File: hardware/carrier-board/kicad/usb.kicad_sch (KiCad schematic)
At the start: 5 parts, among them J11 backpack uplink, J40 RP2350 audio, J41 knob/LoRa, J42 VITURE/cam, U7 USB2514B

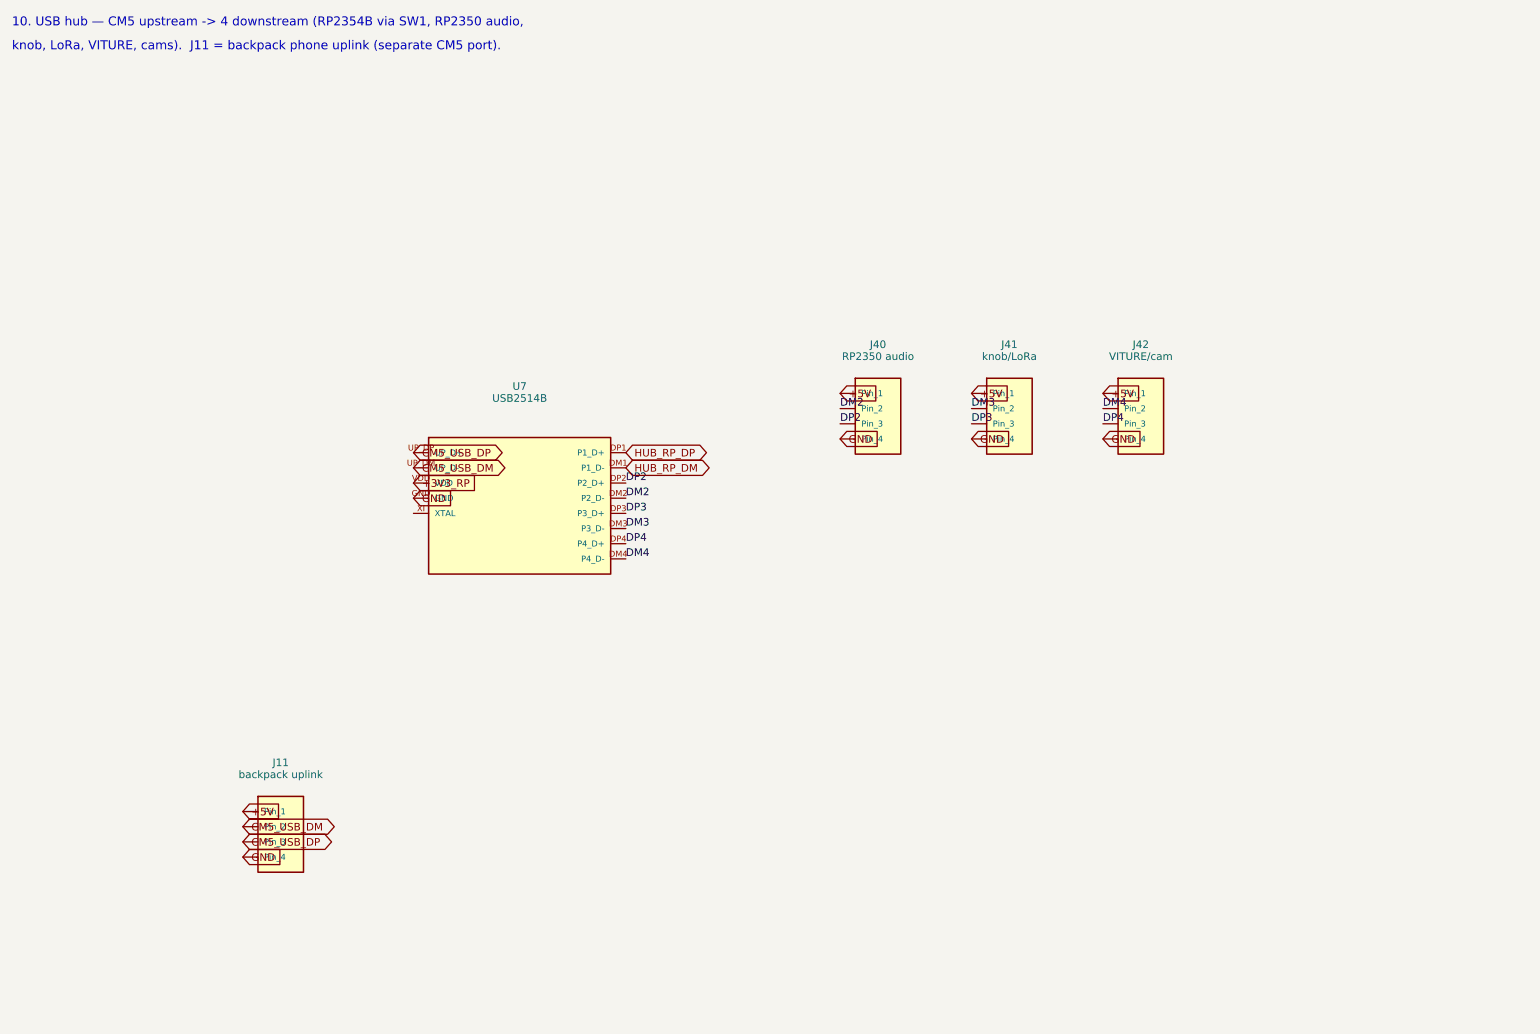
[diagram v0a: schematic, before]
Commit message: hardware(carrier): replace USB 2.0 hub with VL817 USB 3.1 4-port hub
Swap the on-board USB2514B (USB 2.0) for a VIA VL817 4-port USB 3.1 Gen1
(5 Gbps) hub with four USB-C downstream receptacles (J40-J43), upstream on
a CM5 USB 3.0 port. The CM5 exposes 2x USB 3.0 + 1x USB 2.0, so:

  - USB3 #0 -> VL817 upstream (SuperSpeed + USB 2.0)
  - USB3 #1 -> RP2354B CDC (now OFF-hub, via SW1) -> frees all 4 hub ports
  - USB2    -> backpack phone uplink (J11)

Generator (populate_sheets.py):
  - new VL817 condensed symbol (USB2 + SS per port, xtal, reset, straps)
  - new USB-C 3.1 receptacle symbol (VBUS/GND/CC/D+-/one SS lane)
  - CM5 symbol gains USB3 SuperSpeed pins + 2nd/3rd USB ports
  - rewrite sh_usb(): per-port CC Rp pull-ups (56k, host/DFP), VBUS PTC off
    +5V, USBLC6 ESD, SS AC-coupling caps at each TX, 25 MHz hub clock
  - SW1 'A' side rerouted from hub to the dedicated CM5 USB port

Docs: CONNECTORS, POWER, BOM, REQUIREMENTS, BLOCK-DIAGRAM, READMEs updated
for the USB 3.1 hub, USB-C downstream ports, and off-hub RP2354B link.

All 11 sheets regenerated; S-expressions balanced and cross-sheet global
nets verified consistent.

Co-Authored-By: Claude Opus 4.8 <noreply@anthropic.com>
Claude-Session: https://claude.ai/code/session_01DgiE5SHRCeyk1gvfvshMGa
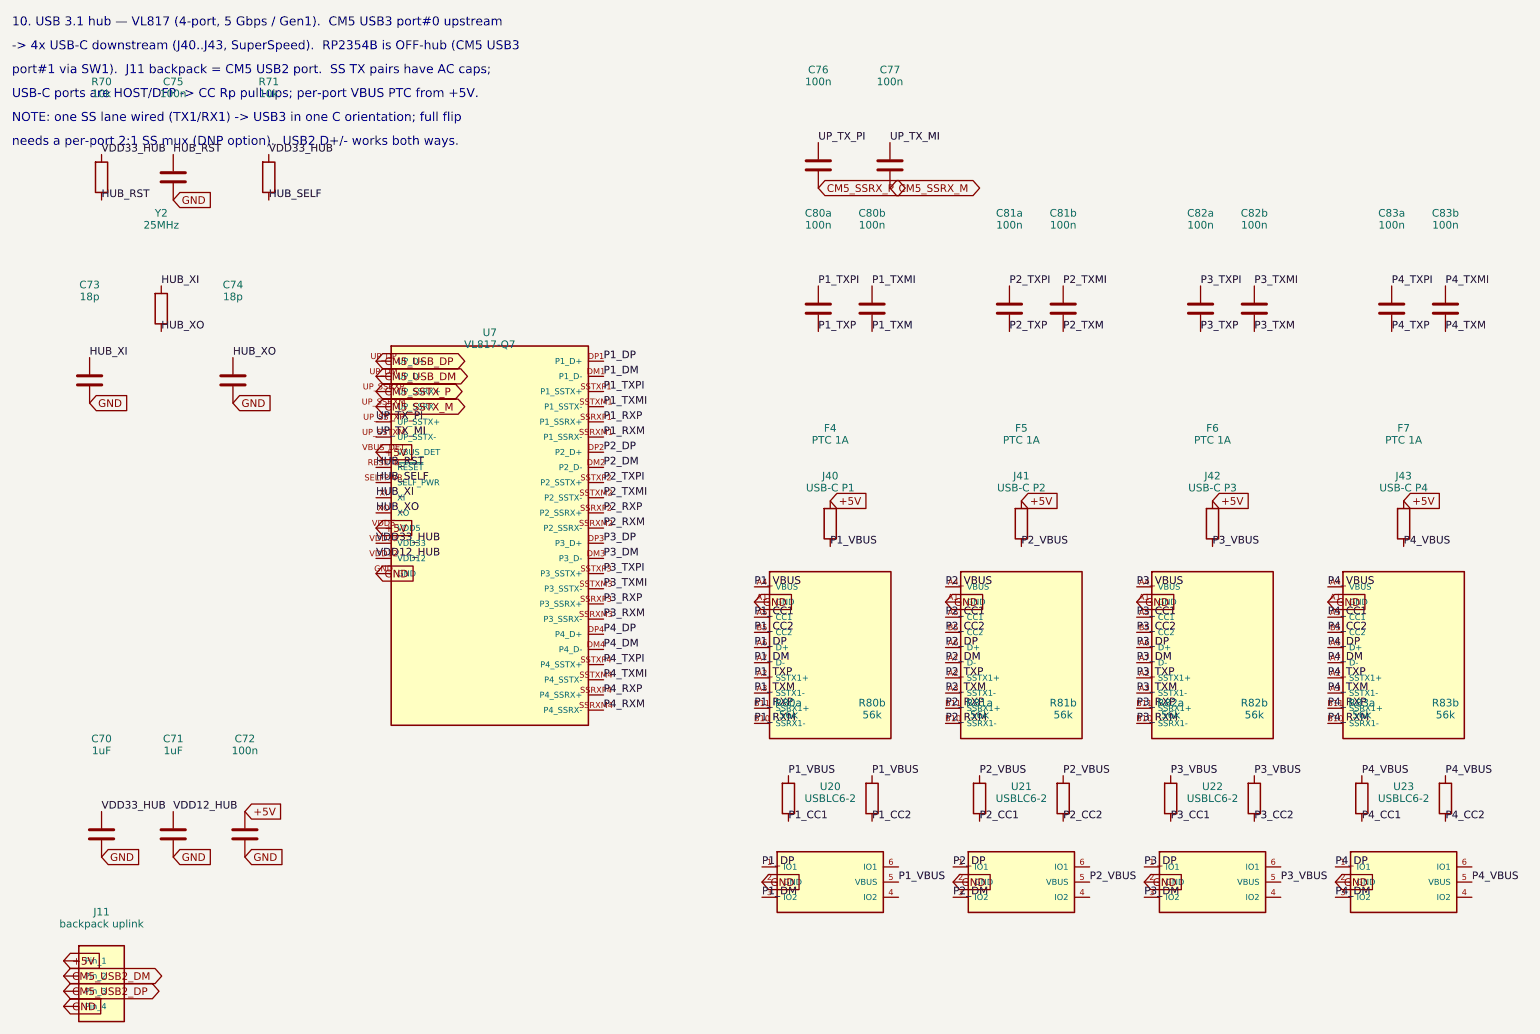
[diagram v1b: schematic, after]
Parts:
- removed J40: RP2350 audio, symbol Connector_Generic:Conn_01x04
- removed J41: knob/LoRa, symbol Connector_Generic:Conn_01x04
- removed J42: VITURE/cam, symbol Connector_Generic:Conn_01x04
- removed U7: USB2514B, symbol Interface_USB:USB2514B
- added C70, C71: 1uF, symbol Device:C
- added C72, C75, C76, C77, C80a, C80b, C81a, C81b, C82a, C82b, C83a, C83b: 100n, symbol Device:C
- added C73, C74: 18p, symbol Device:C
- added F4, F5, F6, F7: PTC 1A, symbol Device:Fuse
- added J40: USB-C P1, symbol Connector:USB_C_Receptacle_USB3.1
- added J41: USB-C P2, symbol Connector:USB_C_Receptacle_USB3.1
- added J42: USB-C P3, symbol Connector:USB_C_Receptacle_USB3.1
- added J43: USB-C P4, symbol Connector:USB_C_Receptacle_USB3.1
- added R70, R71: 10k, symbol Device:R
- added R80a, R80b, R81a, R81b, R82a, R82b, R83a, R83b: 56k, symbol Device:R
- added U20, U21, U22, U23: USBLC6-2, symbol Interface_USB:USBLC6-2SC6
- added U7: VL817-Q7, symbol Interface_USB:VL817
- added Y2: 25MHz, symbol Device:Crystal
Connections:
- net +5V: now also C72.1, F4.1, F5.1, F6.1, F7.1, U7.VBUS_DET, U7.VDD5
- net CM5_USB_DM: now also U7.UP_DM (UP_D-); no longer J11.2 (Pin_2)
- net CM5_USB_DP: now also U7.UP_DP (UP_D+); no longer J11.3 (Pin_3)
- net GND: now also C70.2, C71.2, C72.2, C73.2, C74.2, C75.2, J40.A1 (GND), J41.A1 (GND), J42.A1 (GND), J43.A1 (GND), U20.2 (GND), U21.2 (GND), U22.2 (GND), U23.2 (GND), U7.GND
- new net CM5_SSRX_M: C77.2
- new net CM5_SSRX_P: C76.2
- new net CM5_SSTX_M: U7.UP_SSRXM (UP_SSRX-)
- new net CM5_SSTX_P: U7.UP_SSRXP (UP_SSRX+)
- new net CM5_USB2_DM: J11.2 (Pin_2)
- new net CM5_USB2_DP: J11.3 (Pin_3)
- new net HUB_RST: C75.1, R70.2, U7.RESETB (~{RESET})
- new net HUB_SELF: R71.2, U7.SELFPWR (SELF_PWR)
- new net HUB_XI: C73.1, U7.XI, Y2.1
- new net HUB_XO: C74.1, U7.XO, Y2.2
- new net P1_CC1: J40.A5 (CC1), R80a.2
- new net P1_CC2: J40.B5 (CC2), R80b.2
- new net P1_DM: J40.A7 (D-), U20.3 (IO2), U7.DM1 (P1_D-)
- new net P1_DP: J40.A6 (D+), U20.1 (IO1), U7.DP1 (P1_D+)
- new net P1_RXM: J40.B10 (SSRX1-), U7.SSRXM1 (P1_SSRX-)
- new net P1_RXP: J40.B11 (SSRX1+), U7.SSRXP1 (P1_SSRX+)
- new net P1_TXM: C80b.2, J40.A3 (SSTX1-)
- new net P1_TXMI: C80b.1, U7.SSTXM1 (P1_SSTX-)
- new net P1_TXP: C80a.2, J40.A2 (SSTX1+)
- new net P1_TXPI: C80a.1, U7.SSTXP1 (P1_SSTX+)
- new net P1_VBUS: F4.2, J40.A4 (VBUS), R80a.1, R80b.1, U20.5 (VBUS)
- new net P2_CC1: J41.A5 (CC1), R81a.2
- new net P2_CC2: J41.B5 (CC2), R81b.2
- new net P2_DM: J41.A7 (D-), U21.3 (IO2), U7.DM2 (P2_D-)
- new net P2_DP: J41.A6 (D+), U21.1 (IO1), U7.DP2 (P2_D+)
- new net P2_RXM: J41.B10 (SSRX1-), U7.SSRXM2 (P2_SSRX-)
- new net P2_RXP: J41.B11 (SSRX1+), U7.SSRXP2 (P2_SSRX+)
- new net P2_TXM: C81b.2, J41.A3 (SSTX1-)
- new net P2_TXMI: C81b.1, U7.SSTXM2 (P2_SSTX-)
- new net P2_TXP: C81a.2, J41.A2 (SSTX1+)
- new net P2_TXPI: C81a.1, U7.SSTXP2 (P2_SSTX+)
- new net P2_VBUS: F5.2, J41.A4 (VBUS), R81a.1, R81b.1, U21.5 (VBUS)
- new net P3_CC1: J42.A5 (CC1), R82a.2
- new net P3_CC2: J42.B5 (CC2), R82b.2
- new net P3_DM: J42.A7 (D-), U22.3 (IO2), U7.DM3 (P3_D-)
- new net P3_DP: J42.A6 (D+), U22.1 (IO1), U7.DP3 (P3_D+)
- new net P3_RXM: J42.B10 (SSRX1-), U7.SSRXM3 (P3_SSRX-)
- new net P3_RXP: J42.B11 (SSRX1+), U7.SSRXP3 (P3_SSRX+)
- new net P3_TXM: C82b.2, J42.A3 (SSTX1-)
- new net P3_TXMI: C82b.1, U7.SSTXM3 (P3_SSTX-)
- new net P3_TXP: C82a.2, J42.A2 (SSTX1+)
- new net P3_TXPI: C82a.1, U7.SSTXP3 (P3_SSTX+)
- new net P3_VBUS: F6.2, J42.A4 (VBUS), R82a.1, R82b.1, U22.5 (VBUS)
- new net P4_CC1: J43.A5 (CC1), R83a.2
- new net P4_CC2: J43.B5 (CC2), R83b.2
- new net P4_DM: J43.A7 (D-), U23.3 (IO2), U7.DM4 (P4_D-)
- new net P4_DP: J43.A6 (D+), U23.1 (IO1), U7.DP4 (P4_D+)
- new net P4_RXM: J43.B10 (SSRX1-), U7.SSRXM4 (P4_SSRX-)
- new net P4_RXP: J43.B11 (SSRX1+), U7.SSRXP4 (P4_SSRX+)
- new net P4_TXM: C83b.2, J43.A3 (SSTX1-)
- new net P4_TXMI: C83b.1, U7.SSTXM4 (P4_SSTX-)
- new net P4_TXP: C83a.2, J43.A2 (SSTX1+)
- new net P4_TXPI: C83a.1, U7.SSTXP4 (P4_SSTX+)
- new net P4_VBUS: F7.2, J43.A4 (VBUS), R83a.1, R83b.1, U23.5 (VBUS)
- new net UP_TX_MI: C77.1, U7.UP_SSTXM (UP_SSTX-)
- new net UP_TX_PI: C76.1, U7.UP_SSTXP (UP_SSTX+)
- new net VDD12_HUB: C71.1, U7.VDD12
- new net VDD33_HUB: C70.1, R70.1, R71.1, U7.VDD33
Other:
- note added: "-> 4x USB-C downstream (J40..J43, SuperSpeed). RP2354B is OFF-hub (CM5 USB3"
- note added: "10. USB 3.1 hub — VL817 (4-port, 5 Gbps / Gen1). CM5 USB3 port#0 upstream"
- note added: "NOTE: one SS lane wired (TX1/RX1) -> USB3 in one C orientation; full flip"
- note added: "USB-C ports are HOST/DFP -> CC Rp pull-ups; per-port VBUS PTC from +5V."
- note added: "needs a per-port 2:1 SS mux (DNP option). USB2 D+/- works both ways."
- note added: "port#1 via SW1). J11 backpack = CM5 USB2 port. SS TX pairs have AC caps;"
- note removed: "10. USB hub — CM5 upstream -> 4 downstream (RP2354B via SW1, RP2350 audio,"
- note removed: "knob, LoRa, VITURE, cams). J11 = backpack phone uplink (separate CM5 port)."
- title: ProtoHUD Carrier — 10. USB Hub -> ProtoHUD Carrier — 10. USB 3.1 Hub (VL817)
